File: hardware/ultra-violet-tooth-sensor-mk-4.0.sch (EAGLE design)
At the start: 10 parts, among them IC1 SI1145QFN10, U1 ADAFRUIT_BLUEFRUIT_LE_MICRO, U2 ADAFRUIT-SI1145-BREAKOUTHOLEY

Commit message: simblee based uvdosimeter
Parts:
- removed BATT: M02PTH-CENTERED-R+, A_butts:M02PTH-CENTERED-R+
- removed IC1: SI1145QFN10, A_butts:SI1145QFN10
- removed POWER: SWITCH-SPDTPTH-RA-2.54MM, A_butts:SWITCH-SPDTPTH-RA-2.54MM
- added BAT: M02JST-PTH-RA-R+, a_parts:M02JST-PTH-RA-R+
- added C3, C8: 10u, a_parts:CAPACITOR-CERAMICC0603
- added C4: 10nF, a_parts:CAPACITOR-CERAMICC0603
- added C5: 4u7, a_parts:CAPACITOR-CERAMICC0603
- added C6: 100n, a_parts:CAPACITOR-CERAMICC0603
- added C7: 0.1uF, a_parts:CAPACITOR-CERAMICC0603
- added CHRG, DONE: LED0603, a_parts:LED0603
- added D1: (no value), a_parts:DIODE-SCHOTTKYSOD123
- added DISP1: ER-OLED0.49-1FOLDED-SAME, a_parts:ER-OLED0.49-1FOLDED-SAME
- added Q1: (no value), a_parts:MOSFET-PCHANNELSOT-23
- added R1: 10K, a_parts:RESISTORR0603
- added R4: 1K, a_parts:RESISTORR0603
- added R5: 100K, a_parts:RESISTORR0603
- added RESET: SPST-NO-TACTSMD-TINIER, a_parts:SPST-NO-TACTSMD-TINIER
- added U3: MCP73831T-2ACI/OT, a_parts:MCP73831T-2ACI/OT
- added U4: V_REG_SOT-23-5AS13985, a_parts:V_REG_SOT-23-5AS13985
- added U5: VEML6075, a_parts:VEML6075
- added U6: TCS3400DFN6, a_parts:TCS3400DFN6
- added USB: (no value), a_parts:USB-ABFCI-10103594-USB-MICRO-B-LESS
- C1: device A_butts:CAPACITOR-CERAMICC0805 -> a_parts:CAPACITOR-CERAMICC0603
- C2: value 0.1uF -> 10u; device A_butts:CAPACITOR-CERAMICC0805 -> a_parts:CAPACITOR-CERAMICC0603
- FRAME1: value (none) -> FRAME-LETTERNO_PACKAGE
- R2: value 100k -> 330R; device A_butts:RESISTORR0805 -> a_parts:RESISTORR0603
- R3: value 100k -> 2K; device A_butts:RESISTORR0805 -> a_parts:RESISTORR0603
- U1: value ADAFRUIT_BLUEFRUIT_LE_MICRO -> SIMBLEE-RFD77101; device A_butts:ADAFRUIT_BLUEFRUIT_LE_MICRO -> a_parts:SIMBLEE-RFD77101
- U2: value ADAFRUIT-SI1145-BREAKOUTHOLEY -> FTS31XS-U; device A_butts:ADAFRUIT-SI1145-BREAKOUTHOLEY -> a_parts:FT231XS
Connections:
- removed net SCL: IC1.SCL, R3.1, U1.3/SCL, U2.SCL
- removed net SDA: IC1.SDA, R2.1, U1.2/SDA, U2.SDA
- new net DTR: C4.1
- new net N$2: CHRG.C, DONE.A, R2.1
- new net N$3: U2.USBDP, USB.D+
- new net N$4: U2.USBDM, USB.D-
- new net N$5: R3.2, U3.PROG
- new net N$6: R2.2, U3.STAT
- new net N$9: C6.1, U4.BYPASS
- new net RESET: C4.2, R1.1, RESET.2, U1.RESET/SWDIO
- new net VBAT: BAT.2, C5.1, Q1.D, U3.VBAT
- new net VIN: C2.1, D1.C, Q1.S, U4.EN, U4.IN
- new net VUSB: CHRG.A, D1.A, Q1.G, R5.2, U2.VCC, U3.VDD, USB.VBUS
- net 3.3V: now also C3.1, C7.1, R1.2, U1.VDD, U2.!RESET, U2.VCCIO, U4.OUT; no longer C2.1, IC1.VCC, R2.2, R3.2, U1.3V, U2.3V3_OUT
- net GND: now also BAT.1, C3.2, C5.2, C6.2, C7.2, DONE.C, R3.1, R5.1, RESET.1, U1.GND@1, U1.GND@19, U1.GND@2, U1.GND@30, U1.GND@4, U1.GND@6, U1.PGND@42, U1.PGND@43, U1.PGND@44, U1.PGND@45, U2.GND@16, U2.GND@6, U3.VSS, U4.GND, USB.GND; no longer IC1.GND, U1.GND, U2.GND
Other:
- moved on the sheet: C1, C2, R2, R3

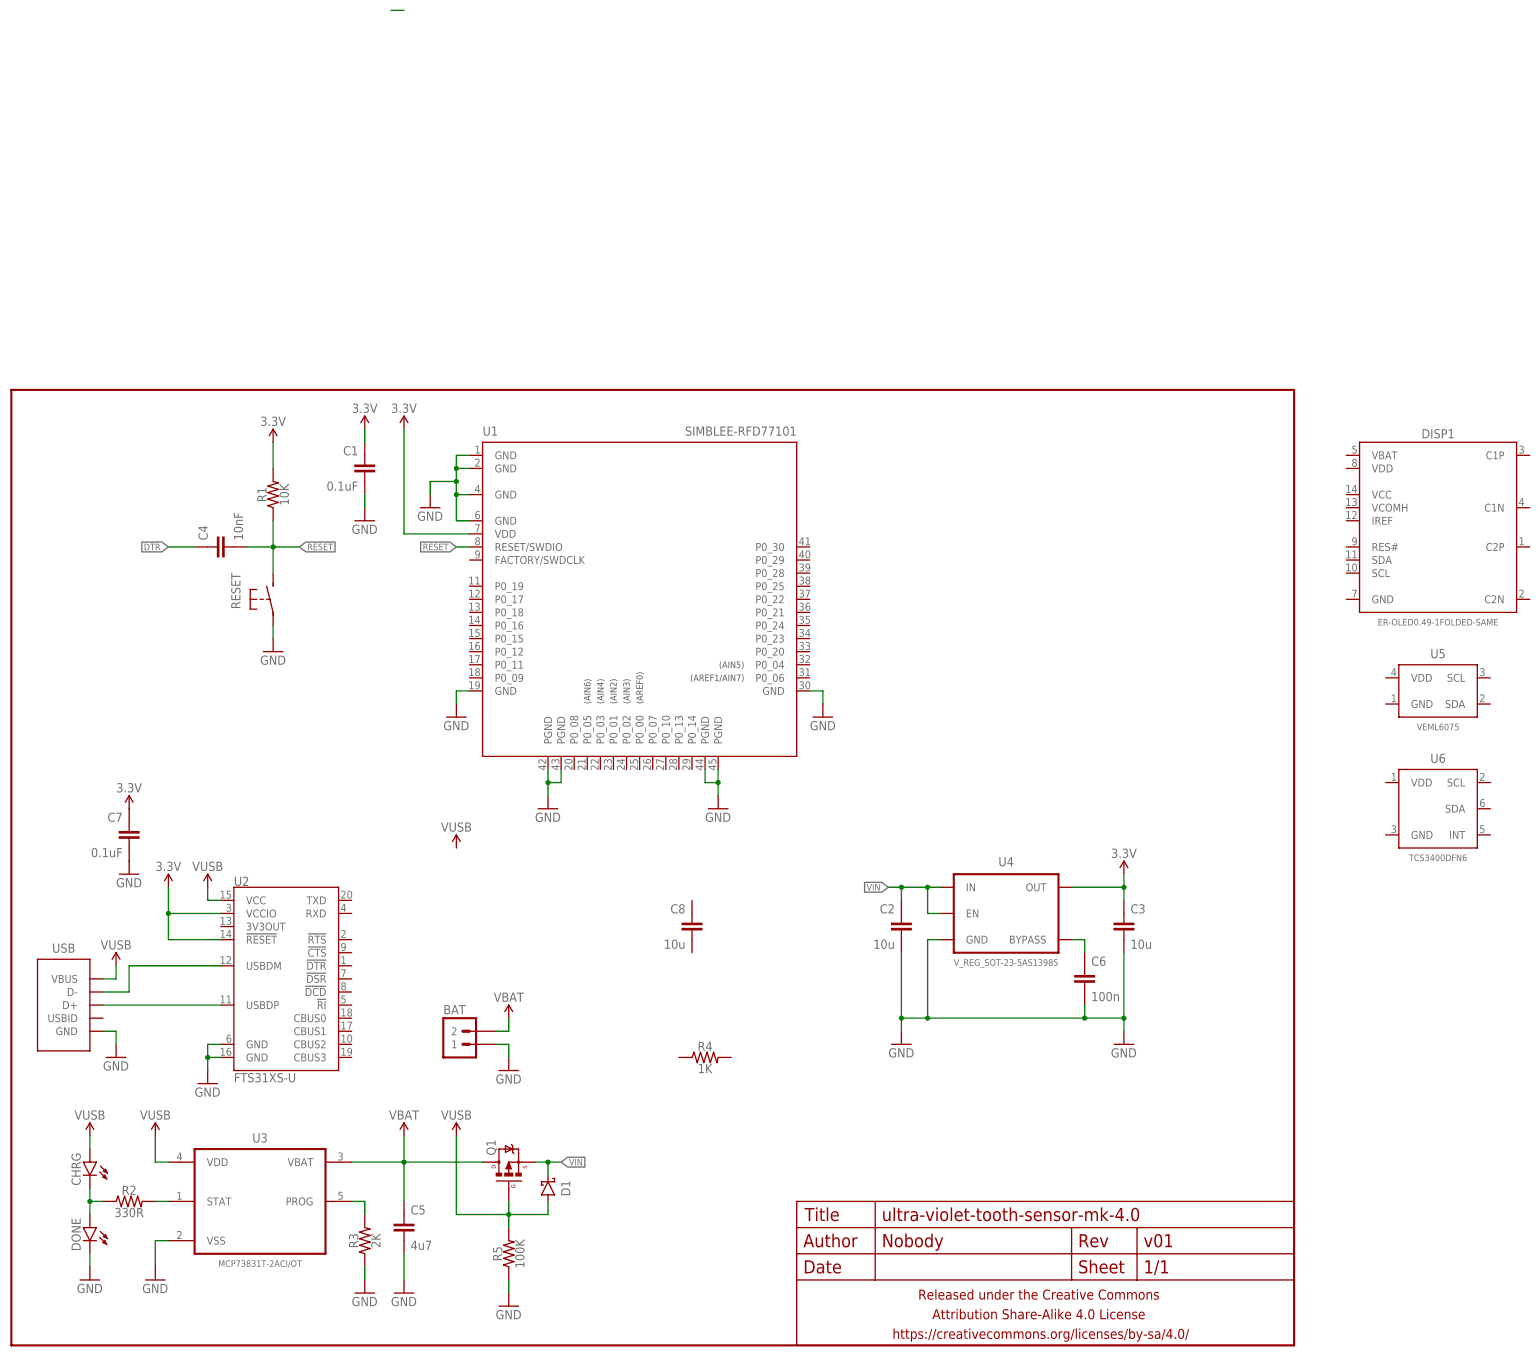
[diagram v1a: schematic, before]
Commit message: more fiddling, need smaller usb to uart chip
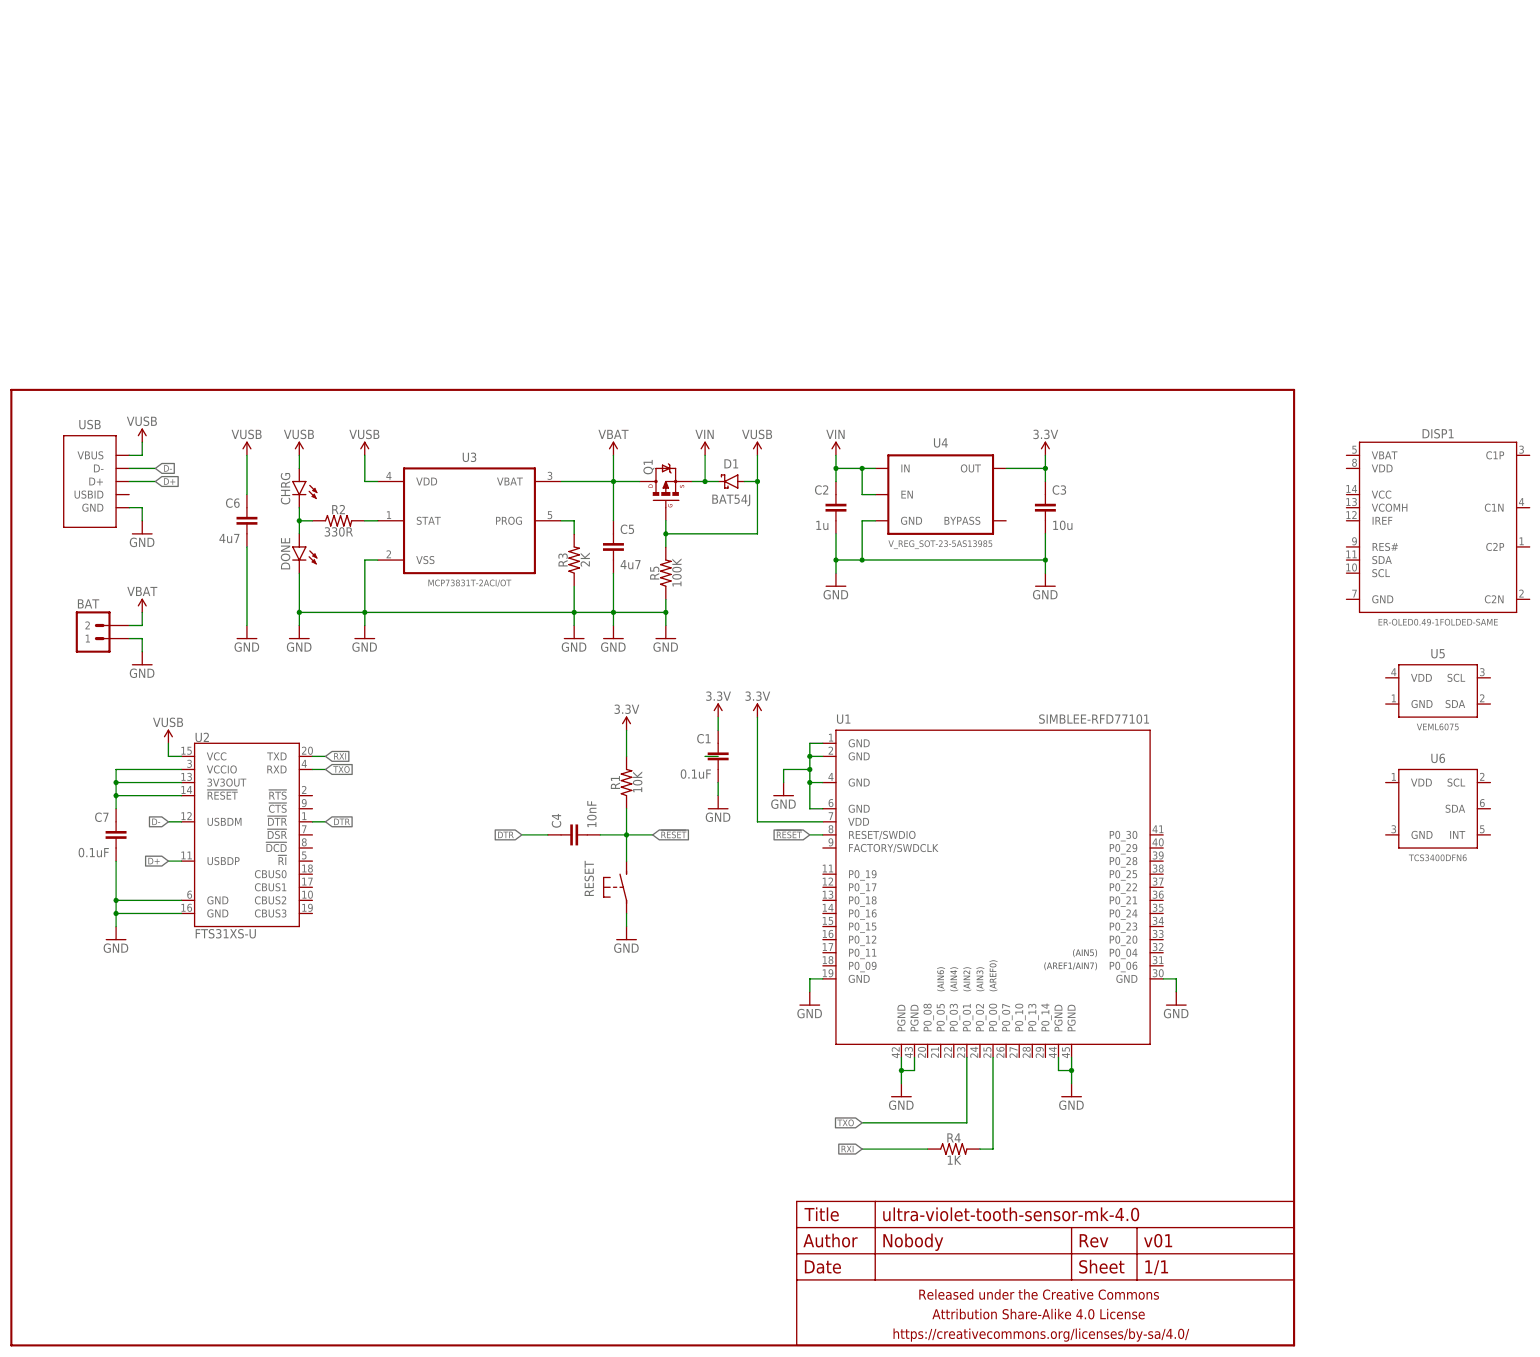
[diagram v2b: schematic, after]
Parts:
- removed C8: 10u, a_parts:CAPACITOR-CERAMICC0603
- BAT: value M02JST-PTH-RA-R+ -> M02JST-PH-VERT-R+; device a_parts:M02JST-PTH-RA-R+ -> a_parts:M02JST-PH-VERT-R+
- C1, C4, C7: device a_parts:CAPACITOR-CERAMICC0603 -> a_parts:CAPACITOR-CERAMICC0402
- C2: value 10u -> 1u; device a_parts:CAPACITOR-CERAMICC0603 -> a_parts:CAPACITOR-CERAMICC0402
- C6: value 100n -> 4u7
- D1: value (none) -> BAT54J; device a_parts:DIODE-SCHOTTKYSOD123 -> a_parts:DIODE-SCHOTTKYSOD323
- R1, R2, R3, R4, R5: device a_parts:RESISTORR0603 -> a_parts:RESISTORR0402
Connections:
- net N$3 renamed D+
- net N$4 renamed D-
- net RESET renamed !RESET
- removed net N$9: C6.1, U4.BYPASS
- new net N$3: R4.2, U1.P0_00
- new net N$4: C7.1, U2.!RESET, U2.3V3OUT, U2.VCCIO
- new net RXI: R4.1, U2.TXD
- new net TXO: U1.P0_01, U2.RXD
- net 3.3V: no longer C7.1, U2.!RESET, U2.VCCIO
- net DTR: now also U2.!DTR
- net VUSB: now also C6.1
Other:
- moved on the sheet: BAT, C1, C2, C3, C4, C5, C6, C7, CHRG, D1, DONE, Q1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

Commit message: new board work
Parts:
- removed DONE: LED0603, a_parts:LED0603
- BAT: value M02JST-PH-VERT-R+ -> M02JST-2MM-SMT; device a_parts:M02JST-PH-VERT-R+ -> a_parts:M02JST-2MM-SMT
- C2: device a_parts:CAPACITOR-CERAMICC0402 -> a_parts:CAPACITOR-CERAMICC0603-TIGHTER
- C3, C5, C6: device a_parts:CAPACITOR-CERAMICC0603 -> a_parts:CAPACITOR-CERAMICC0603-TIGHTER
- CHRG: value LED0603 -> LED0603-TIGHT; device a_parts:LED0603 -> a_parts:LED0603-TIGHT
- U4: value V_REG_SOT-23-5AS13985 -> V_REG_SOT-23-5SPX3819; device a_parts:V_REG_SOT-23-5AS13985 -> a_parts:V_REG_SOT-23-5SPX3819
- USB: value (none) -> USB-AB-SHIELDFCI-10118193-USB-MICRO-B; device a_parts:USB-ABFCI-10103594-USB-MICRO-B-LESS -> a_parts:USB-AB-SHIELDFCI-10118193-USB-MICRO-B
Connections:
- net GND: no longer DONE.C
- net N$2: no longer DONE.A
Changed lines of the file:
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@@
 <part name="GND1" library="a_parts" deviceset="GND" device=""/>
 <part name="C1" library="a_parts" deviceset="CAPACITOR-CERAMIC" device="C0402" value="0.1uF"/>
-<part name="C2" library="a_parts" deviceset="CAPACITOR-CERAMIC" device="C0402" value="1u"/>
+<part name="C2" library="a_parts" deviceset="CAPACITOR-CERAMIC" device="C0603-TIGHTER" value="1u"/>
 <part name="SUPPLY1" library="a_parts" deviceset="3.3V" device=""/>
 <part name="GND5" library="a_parts" deviceset="GND" device=""/>
@@
 <part name="SUPPLY2" library="a_parts" deviceset="3.3V" device=""/>
 <part name="U2" library="a_parts" deviceset="FT231X" device="S" value="FTS31XS-U"/>
-<part name="USB" library="a_parts" deviceset="USB-AB" device="FCI-10103594-USB-MICRO-B-LESS"/>
+<part name="USB" library="a_parts" deviceset="USB-AB-SHIELD" device="FCI-10118193-USB-MICRO-B"/>
 <part name="U5" library="a_parts" deviceset="VEML6075" device=""/>
 <part name="SUPPLY5" library="a_parts" deviceset="VUSB" device=""/>
@@
 <part name="SUPPLY6" library="a_parts" deviceset="VBAT" device=""/>
 <part name="D1" library="a_parts" deviceset="DIODE-SCHOTTKY" device="SOD323" value="BAT54J"/>
-<part name="BAT" library="a_parts" deviceset="M02" device="JST-PH-VERT-R+" value="M02JST-PH-VERT-R+"/>
+<part name="BAT" library="a_parts" deviceset="M02" device="JST-2MM-SMT" value="M02JST-2MM-SMT"/>
 <part name="DISP1" library="a_parts" deviceset="ER-OLED0.49-1" device="FOLDED-SAME"/>
 <part name="Q1" library="a_parts" deviceset="MOSFET-PCHANNEL" device="SOT-23"/>
-<part name="U4" library="a_parts" deviceset="V_REG_SOT-23-5" device="AS13985"/>
+<part name="U4" library="a_parts" deviceset="V_REG_SOT-23-5" device="SPX3819" value="V_REG_SOT-23-5SPX3819"/>
 <part name="GND2" library="a_parts" deviceset="GND" device=""/>
 <part name="GND3" library="a_parts" deviceset="GND" device=""/>
 <part name="SUPPLY7" library="a_parts" deviceset="VUSB" device=""/>
-<part name="CHRG" library="a_parts" deviceset="LED" device="0603"/>
-<part name="DONE" library="a_parts" deviceset="LED" device="0603"/>
+<part name="CHRG" library="a_parts" deviceset="LED" device="0603-TIGHT" value="LED0603-TIGHT"/>
 <part name="R3" library="a_parts" deviceset="RESISTOR" device="R0402" value="2K"/>
 <part name="SUPPLY8" library="a_parts" deviceset="3.3V" device=""/>
-<part name="C3" library="a_parts" deviceset="CAPACITOR-CERAMIC" device="C0603" value="10u"/>
+<part name="C3" library="a_parts" deviceset="CAPACITOR-CERAMIC" device="C0603-TIGHTER" value="10u"/>
 <part name="GND4" library="a_parts" deviceset="GND" device=""/>
 <part name="GND6" library="a_parts" deviceset="GND" device=""/>
@@
 <part name="R2" library="a_parts" deviceset="RESISTOR" device="R0402" value="330R"/>
 <part name="SUPPLY10" library="a_parts" deviceset="VUSB" device=""/>
-<part name="GND12" library="a_parts" deviceset="GND" device=""/>
 <part name="R5" library="a_parts" deviceset="RESISTOR" device="R0402" value="100K"/>
 <part name="GND13" library="a_parts" deviceset="GND" device=""/>
 <part name="SUPPLY11" library="a_parts" deviceset="VUSB" device=""/>
-<part name="C5" library="a_parts" deviceset="CAPACITOR-CERAMIC" device="C0603" value="4u7"/>
+<part name="C5" library="a_parts" deviceset="CAPACITOR-CERAMIC" device="C0603-TIGHTER" value="4u7"/>
 <part name="GND14" library="a_parts" deviceset="GND" device=""/>
 <part name="GND15" library="a_parts" deviceset="GND" device=""/>
@@
 <part name="GND19" library="a_parts" deviceset="GND" device=""/>
 <part name="R4" library="a_parts" deviceset="RESISTOR" device="R0402" value="1K"/>
-<part name="C6" library="a_parts" deviceset="CAPACITOR-CERAMIC" device="C0603" value="4u7"/>
+<part name="C6" library="a_parts" deviceset="CAPACITOR-CERAMIC" device="C0603-TIGHTER" value="4u7"/>
 </parts>
 <sheets>
@@
 <instance part="SUPPLY7" gate="G$1" x="30.48" y="116.84"/>
 <instance part="CHRG" gate="G$1" x="55.88" y="167.64" rot="MR0"/>
-<instance part="DONE" gate="G$1" x="55.88" y="154.94" rot="MR0"/>
 <instance part="R3" gate="G$1" x="109.22" y="152.4" rot="R90"/>
 <instance part="SUPPLY8" gate="G$1" x="119.38" y="119.38"/>
@@
 <instance part="R2" gate="G$1" x="63.5" y="160.02"/>
 <instance part="SUPPLY10" gate="G$1" x="55.88" y="172.72"/>
-<instance part="GND12" gate="1" x="55.88" y="137.16"/>
 <instance part="R5" gate="G$1" x="127" y="149.86" rot="R90"/>
 <instance part="GND13" gate="1" x="127" y="137.16"/>
@@
 <pinref part="GND4" gate="1" pin="GND"/>
 <wire x1="68.58" y1="152.4" x2="68.58" y2="142.24" width="0.1524" layer="91"/>
-<pinref part="DONE" gate="G$1" pin="C"/>
-<pinref part="GND12" gate="1" pin="GND"/>
 <wire x1="68.58" y1="142.24" x2="68.58" y2="139.7" width="0.1524" layer="91"/>
-<wire x1="55.88" y1="139.7" x2="55.88" y2="142.24" width="0.1524" layer="91"/>
-<wire x1="55.88" y1="142.24" x2="55.88" y2="149.86" width="0.1524" layer="91"/>
-<wire x1="68.58" y1="142.24" x2="55.88" y2="142.24" width="0.1524" layer="91"/>
 <junction x="68.58" y="142.24"/>
-<junction x="55.88" y="142.24"/>
 <pinref part="R3" gate="G$1" pin="1"/>
 <pinref part="GND11" gate="1" pin="GND"/>
@@
 <net name="N$2" class="0">
 <segment>
-<pinref part="DONE" gate="G$1" pin="A"/>
 <pinref part="CHRG" gate="G$1" pin="C"/>
-<wire x1="55.88" y1="157.48" x2="55.88" y2="160.02" width="0.1524" layer="91"/>
 <pinref part="R2" gate="G$1" pin="1"/>
 <wire x1="55.88" y1="160.02" x2="55.88" y2="162.56" width="0.1524" layer="91"/>
 <wire x1="55.88" y1="160.02" x2="58.42" y2="160.02" width="0.1524" layer="91"/>
-<junction x="55.88" y="160.02"/>
-</segment>
-</net>
+</segment>
+</net>
